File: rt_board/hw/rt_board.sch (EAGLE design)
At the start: 71 parts, among them IC1 MCP170333MB, IC2/L1 TLE4935L, IC3/L2 TLE4935L, IC4/R1 TLE4935L, IC5/R2 TLE4935L, Q1 8MHz, SW2 B3U-1000PM-B, U1 DRV8801PWP, U2 DRV8801PWP, U3 SN74AVC4T245PW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

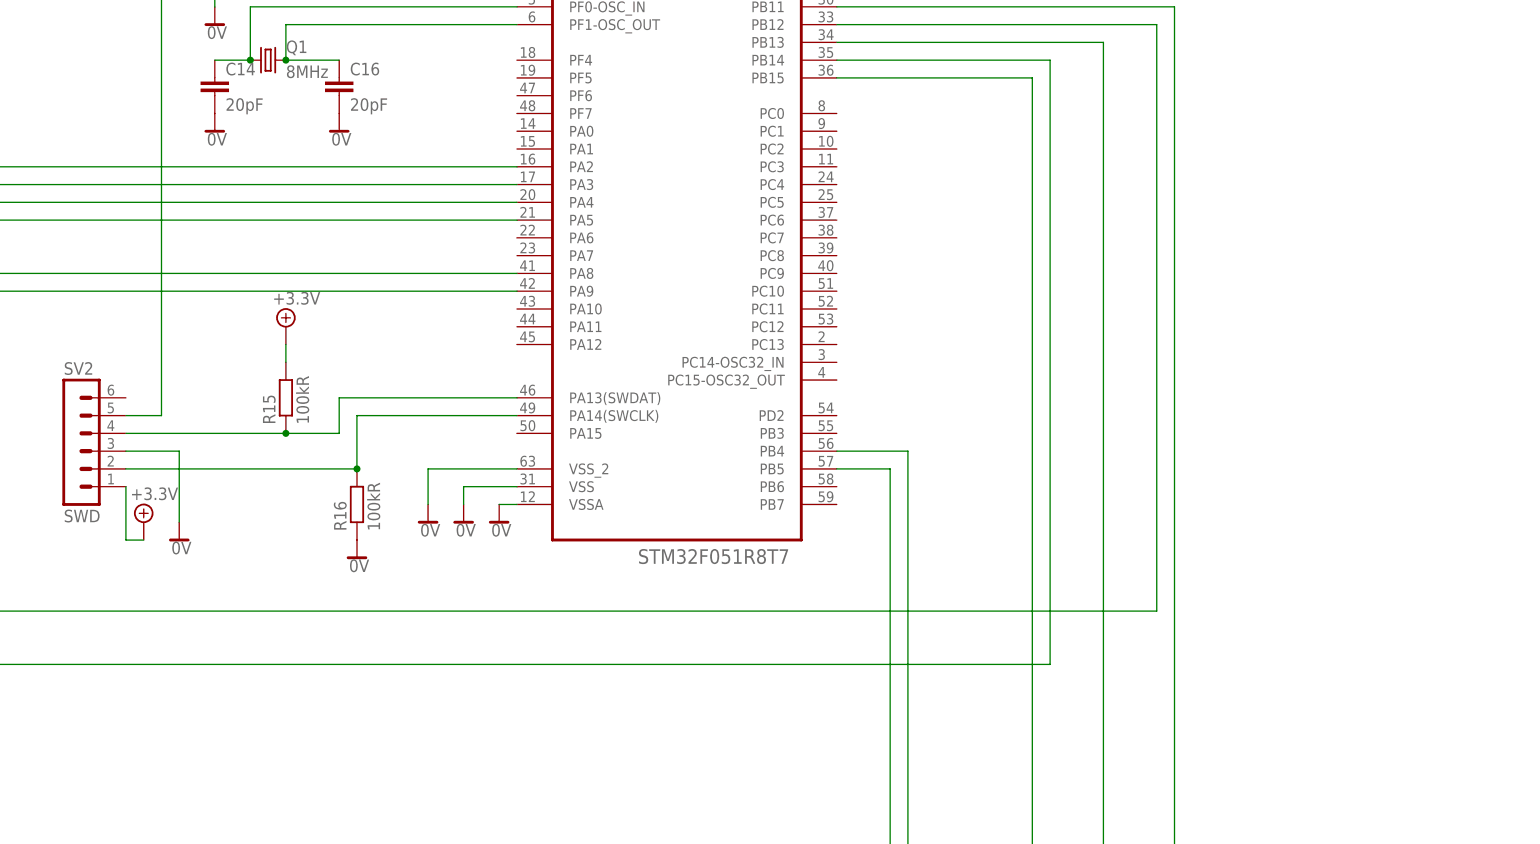
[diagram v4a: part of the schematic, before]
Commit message: added Ext-1 pinhead with power supply and ground (4 gpios)
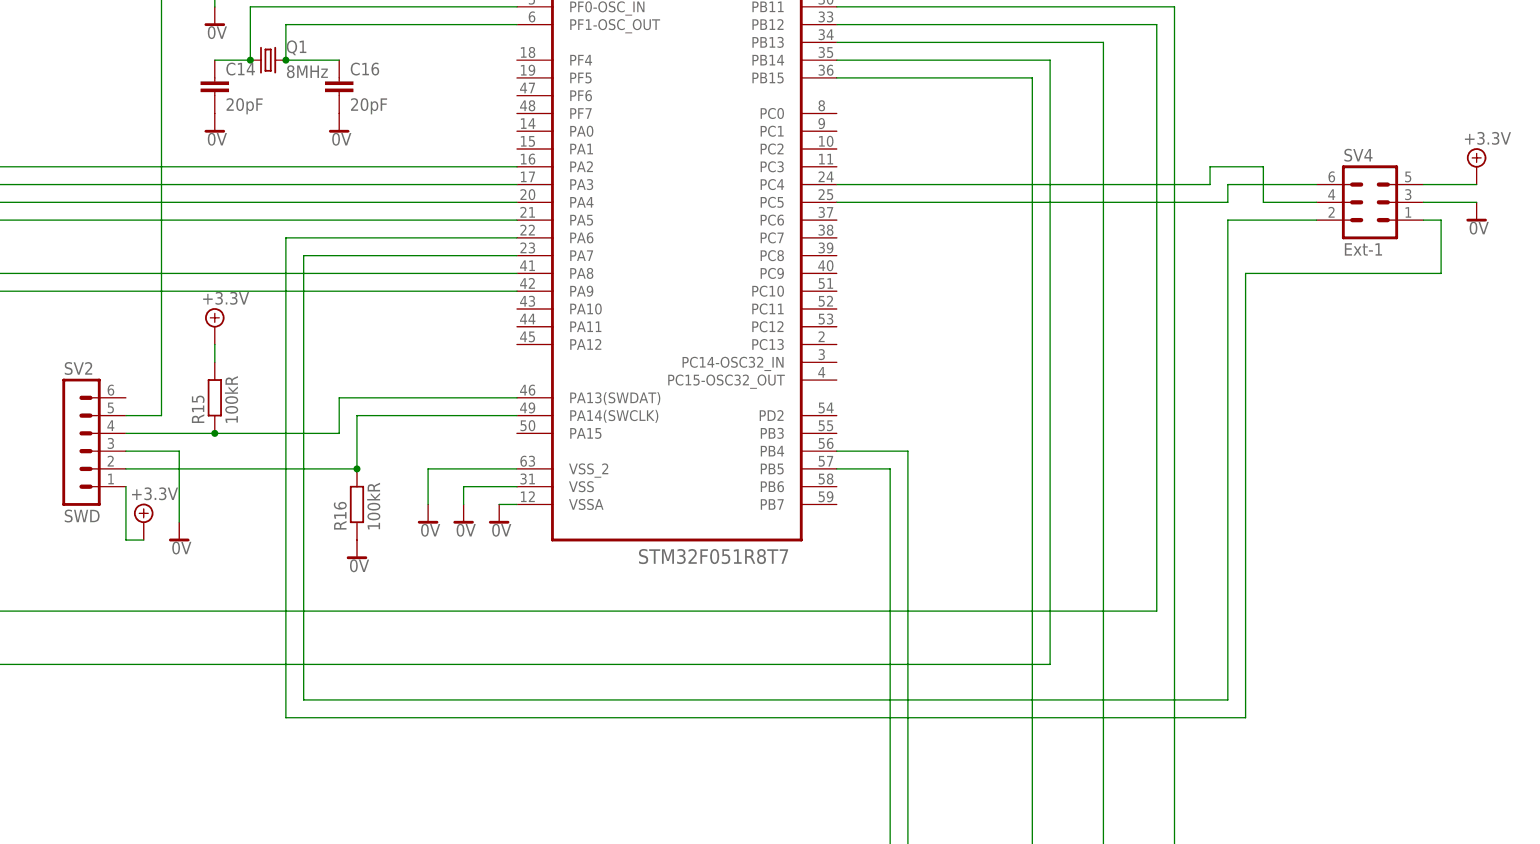
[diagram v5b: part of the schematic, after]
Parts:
- added SV4: Ext-1, con-lstb:MA03-2
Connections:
- new net N$52: SV4.6, U6.PC5
- new net N$53: SV4.4, U6.PC4
- new net N$54: SV4.2, U6.PA7
- new net N$55: SV4.1, U6.PA6
- net +5V: now also SV4.5
- net 0V: now also SV4.3
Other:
- moved on the sheet: R15
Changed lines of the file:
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@@
 <part name="SUPPLY95" library="supply2" deviceset="0V" device=""/>
 <part name="SUPPLY96" library="supply2" deviceset="0V" device=""/>
+<part name="SUPPLY98" library="supply2" deviceset="0V" device=""/>
+<part name="SV4" library="con-lstb" deviceset="MA03-2" device="" value="Ext-1"/>
+<part name="SUPPLY85" library="supply2" deviceset="+5V" device="" value="+3.3V"/>
 </parts>
 <sheets>
@@
 <instance part="R16" gate="G$1" x="-48.26" y="-5.08" rot="R90"/>
 <instance part="SUPPLY35" gate="0V" x="-48.26" y="-12.7"/>
-<instance part="R15" gate="G$1" x="-58.42" y="10.16" rot="R90"/>
-<instance part="SUPPLY36" gate="+5V" x="-58.42" y="20.32"/>
+<instance part="R15" gate="G$1" x="-68.58" y="10.16" rot="R90"/>
+<instance part="SUPPLY36" gate="+5V" x="-68.58" y="20.32"/>
 <instance part="U3" gate="A" x="-172.72" y="66.04"/>
 <instance part="SV1" gate="1" x="-129.54" y="111.76" rot="R180"/>
@@
 <instance part="SUPPLY95" gate="0V" x="-228.6" y="-5.08"/>
 <instance part="SUPPLY96" gate="0V" x="-228.6" y="15.24"/>
+<instance part="SUPPLY98" gate="0V" x="111.76" y="35.56"/>
+<instance part="SV4" gate="1" x="96.52" y="38.1"/>
+<instance part="SUPPLY85" gate="+5V" x="111.76" y="43.18"/>
 </instances>
 <busses>
@@
 <wire x1="-228.6" y1="17.78" x2="-233.68" y2="17.78" width="0.1524" layer="91"/>
 </segment>
+<segment>
+<pinref part="SUPPLY98" gate="0V" pin="0V"/>
+<wire x1="111.76" y1="38.1" x2="104.14" y2="38.1" width="0.1524" layer="91"/>
+<pinref part="SV4" gate="1" pin="3"/>
+</segment>
 </net>
 <net name="+5V" class="0">
@@
 <pinref part="R15" gate="G$1" pin="2"/>
 <pinref part="SUPPLY36" gate="+5V" pin="+5V"/>
-<wire x1="-58.42" y1="15.24" x2="-58.42" y2="17.78" width="0.1524" layer="91"/>
+<wire x1="-68.58" y1="15.24" x2="-68.58" y2="17.78" width="0.1524" layer="91"/>
 </segment>
 <segment>
@@
 <pinref part="SUPPLY83" gate="+5V" pin="+5V"/>
 <wire x1="38.1" y1="109.22" x2="38.1" y2="106.68" width="0.1524" layer="91"/>
+</segment>
+<segment>
+<wire x1="111.76" y1="40.64" x2="104.14" y2="40.64" width="0.1524" layer="91"/>
+<pinref part="SV4" gate="1" pin="5"/>
+<pinref part="SUPPLY85" gate="+5V" pin="+5V"/>
 </segment>
 </net>
@@
 <wire x1="-25.4" y1="10.16" x2="-50.8" y2="10.16" width="0.1524" layer="91"/>
 <wire x1="-50.8" y1="10.16" x2="-50.8" y2="5.08" width="0.1524" layer="91"/>
-<wire x1="-50.8" y1="5.08" x2="-58.42" y2="5.08" width="0.1524" layer="91"/>
+<wire x1="-50.8" y1="5.08" x2="-68.58" y2="5.08" width="0.1524" layer="91"/>
 <pinref part="SV2" gate="1" pin="4"/>
-<wire x1="-58.42" y1="5.08" x2="-81.28" y2="5.08" width="0.1524" layer="91"/>
+<wire x1="-68.58" y1="5.08" x2="-81.28" y2="5.08" width="0.1524" layer="91"/>
 <pinref part="R15" gate="G$1" pin="1"/>
-<junction x="-58.42" y="5.08"/>
+<junction x="-68.58" y="5.08"/>
 </segment>
 </net>
@@
 </segment>
 </net>
+<net name="N$52" class="0">
+<segment>
+<pinref part="U6" gate="A" pin="PC5"/>
+<wire x1="20.32" y1="38.1" x2="76.2" y2="38.1" width="0.1524" layer="91"/>
+<wire x1="76.2" y1="38.1" x2="76.2" y2="40.64" width="0.1524" layer="91"/>
+<wire x1="76.2" y1="40.64" x2="88.9" y2="40.64" width="0.1524" layer="91"/>
+<pinref part="SV4" gate="1" pin="6"/>
+</segment>
+</net>
+<net name="N$53" class="0">
+<segment>
+<pinref part="U6" gate="A" pin="PC4"/>
+<wire x1="20.32" y1="40.64" x2="73.66" y2="40.64" width="0.1524" layer="91"/>
+<wire x1="73.66" y1="40.64" x2="73.66" y2="43.18" width="0.1524" layer="91"/>
+<wire x1="73.66" y1="43.18" x2="81.28" y2="43.18" width="0.1524" layer="91"/>
+<wire x1="81.28" y1="43.18" x2="81.28" y2="38.1" width="0.1524" layer="91"/>
+<wire x1="81.28" y1="38.1" x2="88.9" y2="38.1" width="0.1524" layer="91"/>
+<pinref part="SV4" gate="1" pin="4"/>
+</segment>
+</net>
+<net name="N$54" class="0">
+<segment>
+<pinref part="U6" gate="A" pin="PA7"/>
+<wire x1="-25.4" y1="30.48" x2="-55.88" y2="30.48" width="0.1524" layer="91"/>
+<wire x1="-55.88" y1="30.48" x2="-55.88" y2="-33.02" width="0.1524" layer="91"/>
+<wire x1="-55.88" y1="-33.02" x2="76.2" y2="-33.02" width="0.1524" layer="91"/>
+<wire x1="76.2" y1="-33.02" x2="76.2" y2="35.56" width="0.1524" layer="91"/>
+<wire x1="76.2" y1="35.56" x2="88.9" y2="35.56" width="0.1524" layer="91"/>
+<pinref part="SV4" gate="1" pin="2"/>
+</segment>
+</net>
+<net name="N$55" class="0">
+<segment>
+<pinref part="U6" gate="A" pin="PA6"/>
+<wire x1="-25.4" y1="33.02" x2="-58.42" y2="33.02" width="0.1524" layer="91"/>
+<wire x1="-58.42" y1="33.02" x2="-58.42" y2="-35.56" width="0.1524" layer="91"/>
+<wire x1="-58.42" y1="-35.56" x2="78.74" y2="-35.56" width="0.1524" layer="91"/>
+<wire x1="78.74" y1="-35.56" x2="78.74" y2="27.94" width="0.1524" layer="91"/>
+<wire x1="78.74" y1="27.94" x2="106.68" y2="27.94" width="0.1524" layer="91"/>
+<wire x1="106.68" y1="27.94" x2="106.68" y2="35.56" width="0.1524" layer="91"/>
+<wire x1="106.68" y1="35.56" x2="104.14" y2="35.56" width="0.1524" layer="91"/>
+<pinref part="SV4" gate="1" pin="1"/>
+</segment>
+</net>
